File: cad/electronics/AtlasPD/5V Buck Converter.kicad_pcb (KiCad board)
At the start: 2 copper layers, 93.5 x 50.4 mm, 12 parts, among them J401 Conn_01x04, U402 AP1509-50SG-13

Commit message: KiCad 6.0 upgrade
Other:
- net class Default removed

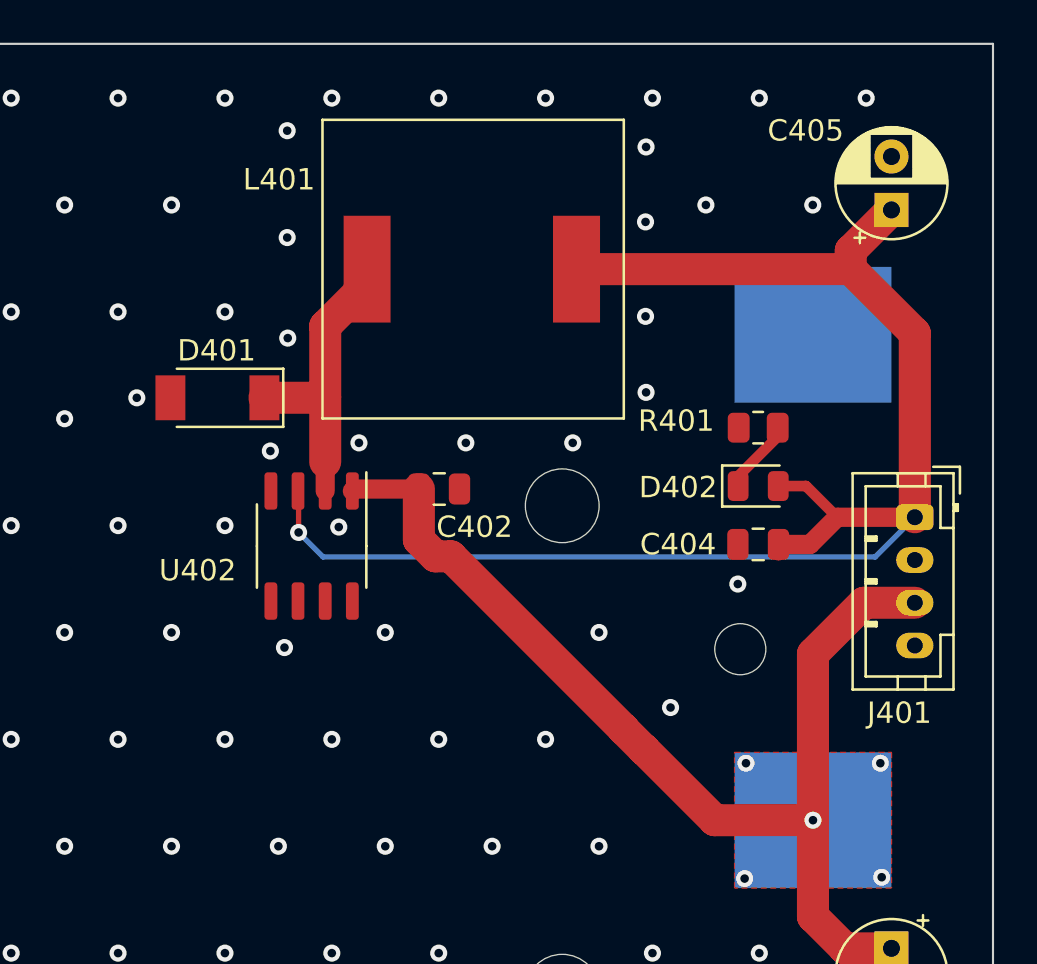
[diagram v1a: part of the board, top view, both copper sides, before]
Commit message: Started adding battery protection and fuel guage design
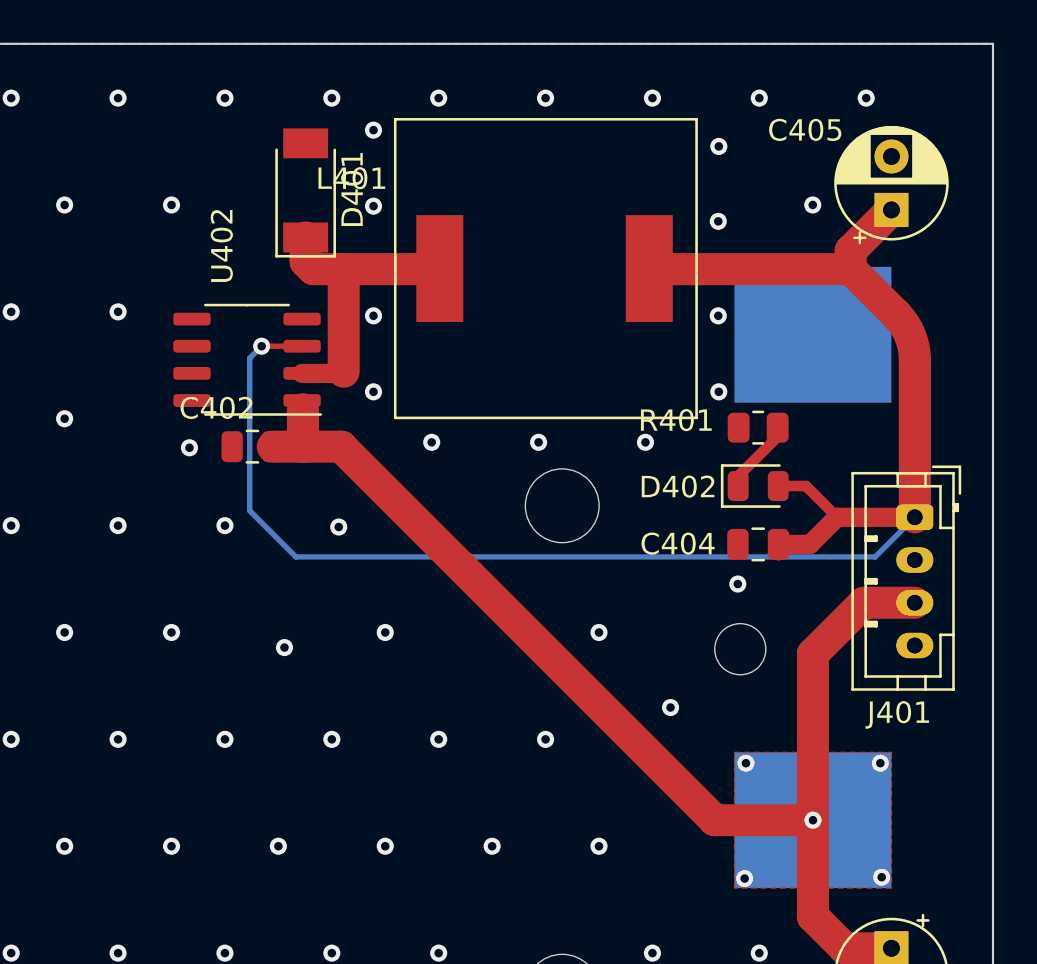
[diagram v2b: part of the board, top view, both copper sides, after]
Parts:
- moved D401 10.5 mm to (76.4, 51.3), turned to 90 degrees
- moved U402 9.22 mm to (73.7, 59.2), turned to 180 degrees
- moved C402 8.96 mm to (73.9, 63.3), turned to 180 degrees
- moved L401 3.40 mm to (87.6, 55.0)
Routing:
- net +5V: track 72.8 -> 79.1 mm
- net +BATT: track 51.7 -> 56.6 mm
- net GND: vias 144 -> 142

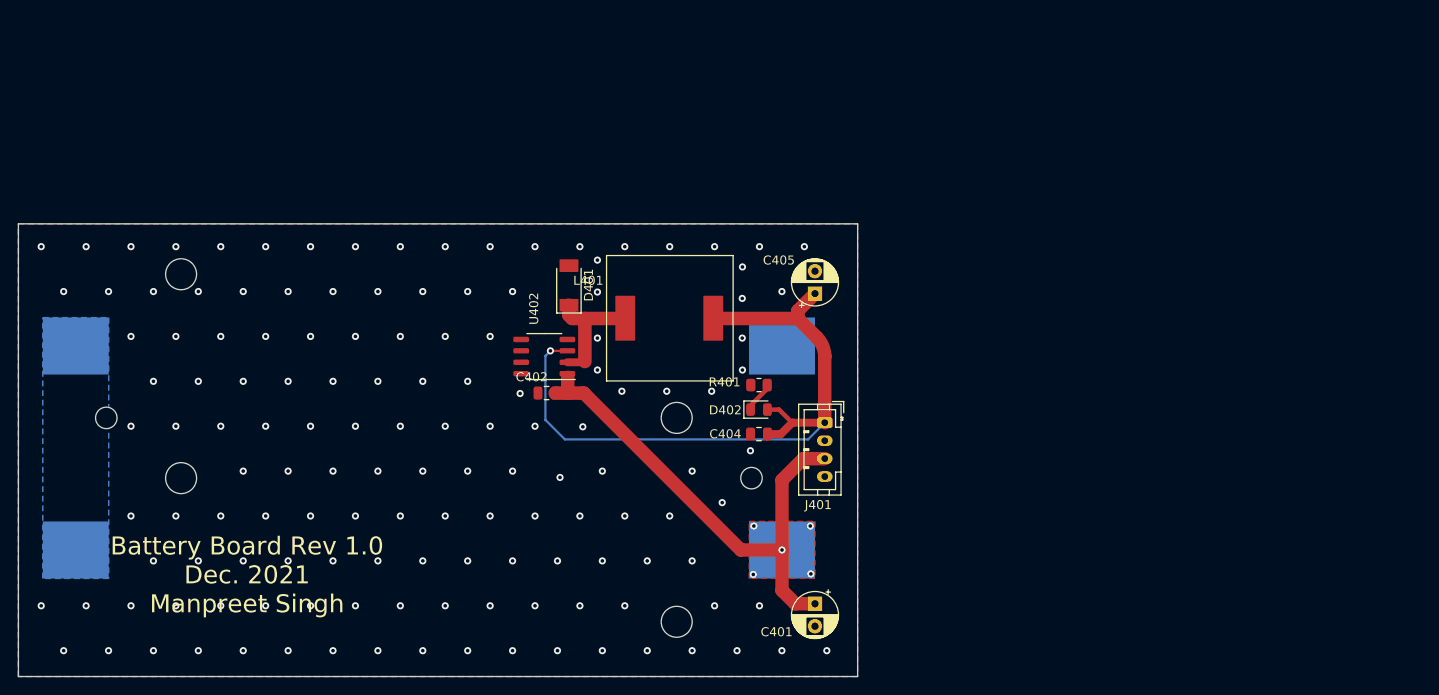
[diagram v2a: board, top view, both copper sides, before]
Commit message: Finished IC Schematic, Assigned footprints
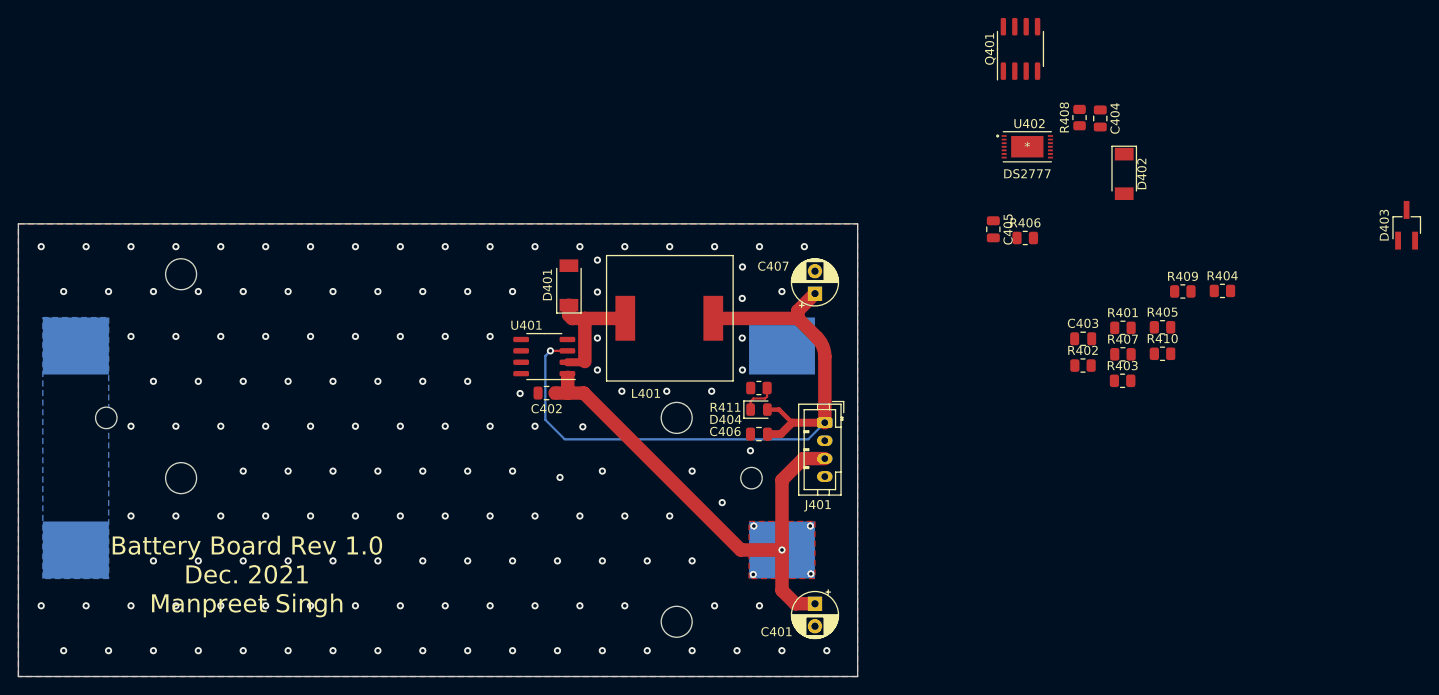
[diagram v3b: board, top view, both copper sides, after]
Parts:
- added C403: 0.1u, Capacitor_SMD:C_0805_2012Metric, F.Cu at (133.7, 57.3)
- added C404: 0.47u, Capacitor_SMD:C_0805_2012Metric, F.Cu at (135.6, 32.7)
- added C405: 0.1u, Capacitor_SMD:C_0805_2012Metric, F.Cu at (123.7, 45.1)
- added D402: D_Schottky, Diode_SMD:D_SOD-128, F.Cu at (138.3, 38.9)
- added D403: D_Zener_Dual_CommonAnode_KKA_Parallel, Package_TO_SOT_SMD:TSOT-23_HandSoldering, F.Cu at (169.7, 44.6)
- added Q401: Q_Dual_NMOS_S1G1S2G2D2D2D1D1, Package_SO:SOIC-8_3.9x4.9mm_P1.27mm, F.Cu at (126.7, 25.0)
- added R401: 1k, Resistor_SMD:R_0805_2012Metric, F.Cu at (138.1, 56.0)
- added R402: 1k, Resistor_SMD:R_0805_2012Metric, F.Cu at (133.7, 60.2)
- added R403: 150, Resistor_SMD:R_0805_2012Metric, F.Cu at (138.1, 61.9)
- added R404: 1k, Resistor_SMD:R_0805_2012Metric, F.Cu at (149.2, 51.9)
- added R405: 470, Resistor_SMD:R_0805_2012Metric, F.Cu at (142.5, 56.0)
- added R406: RSNS, Resistor_SMD:R_0805_2012Metric, F.Cu at (127.3, 46.0)
- added R407: 1k, Resistor_SMD:R_0805_2012Metric, F.Cu at (138.1, 59.0)
- added R408: 1k, Resistor_SMD:R_0805_2012Metric, F.Cu at (133.3, 32.6)
- added R409: 150, Resistor_SMD:R_0805_2012Metric, F.Cu at (144.8, 52.0)
- added R410: 150, Resistor_SMD:R_0805_2012Metric, F.Cu at (142.5, 58.9)
- added U402: DS2777, SamacSys_Parts:DS2777G+, F.Cu at (127.5, 35.9)
- moved R411 0.33 mm to (97.6, 62.7)
- renumbered C404 to C406, C405 to C407, D402 to D404, R401 to R411, U402 to U401
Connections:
- BT401 pad 1: +BATT -> Net-(BT401-Pad1)
- BT402 pad 2: GND -> GNDPWR
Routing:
- net Net-(D404-Pad1): track 3.50 -> 4.80 mm

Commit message: Forgot to save
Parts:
- moved D402 24.6 mm to (113.7, 37.8), turned to 0 degrees
- moved R407 19.4 mm to (133.7, 40.1), turned to 180 degrees
- moved D403 6.48 mm to (164.0, 41.5), turned to -90 degrees
- moved C404 5.67 mm to (133.7, 38.0), turned to 0 degrees
- moved U402 3.26 mm to (124.7, 37.5)
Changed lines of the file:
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@@
   )
   (footprint "Package_TO_SOT_SMD:TSOT-23_HandSoldering" (layer "F.Cu")
-    (at 169.7244 44.6106 90)
+    (at 164.0332 41.5036 -90)
     (descr "5-pin TSOT23 package, http://cds.linear.com/docs/en/packaging/SOT_5_05-08-1635.pdf")
     (tags "TSOT-23 Hand-soldering")
@@
     (fp_line (start -0.88 -1) (end -0.43 -1.45) (layer "F.Fab") (width 0.1))
     (fp_line (start 0.88 -1.45) (end -0.43 -1.45) (layer "F.Fab") (width 0.1))
-    (pad "1" smd rect locked (at -1.71 -0.95 90) (size 2 0.65) (layers "F.Cu" "F.Paste" "F.Mask")
+    (pad "1" smd rect locked (at -1.71 -0.95 270) (size 2 0.65) (layers "F.Cu" "F.Paste" "F.Mask")
       (net 21 "Net-(D403-Pad1)") (pinfunction "K") (pintype "passive"))
-    (pad "2" smd rect locked (at -1.71 0.95 90) (size 2 0.65) (layers "F.Cu" "F.Paste" "F.Mask")
+    (pad "2" smd rect locked (at -1.71 0.95 270) (size 2 0.65) (layers "F.Cu" "F.Paste" "F.Mask")
       (net 23 "Net-(D403-Pad2)") (pinfunction "K") (pintype "passive"))
-    (pad "3" smd rect locked (at 1.71 0 90) (size 2 0.65) (layers "F.Cu" "F.Paste" "F.Mask")
+    (pad "3" smd rect locked (at 1.71 0 270) (size 2 0.65) (layers "F.Cu" "F.Paste" "F.Mask")
       (net 1 "GND") (pinfunction "A") (pintype "passive"))
     (model "${KICAD6_3DMODEL_DIR}/Package_TO_SOT_SMD.3dshapes/TSOT-23.wrl"
@@
   )
   (footprint "Diode_SMD:D_SOD-128" (layer "F.Cu")
-    (at 138.2776 38.8874 -90)
+    (at 113.665 37.7698)
     (descr "D_SOD-128 (CFP5 SlimSMAW), https://assets.nexperia.com/documents/outline-drawing/SOD128.pdf")
     (tags "D_SOD-128")
@@
     (property "Sheetname" "")
     (attr smd)
-    (fp_text reference "D402" (at 0 -2 90) (layer "F.SilkS")
-      (effects (font (size 1 1) (thickness 0.15)))
-    )
-    (fp_text value "D_Schottky" (at 0 2 90) (layer "F.Fab")
-      (effects (font (size 1 1) (thickness 0.15)))
-    )
-    (fp_text user "${REFERENCE}" (at 0 -2 90) (layer "F.Fab")
+    (fp_text reference "D402" (at 0 -2) (layer "F.SilkS")
+      (effects (font (size 1 1) (thickness 0.15)))
+    )
+    (fp_text value "D_Schottky" (at 0 2) (layer "F.Fab")
+      (effects (font (size 1 1) (thickness 0.15)))
+    )
+    (fp_text user "${REFERENCE}" (at 0 -2) (layer "F.Fab")
       (effects (font (size 1 1) (thickness 0.15)))
     )
@@
     (fp_line (start 1.9 1.25) (end -1.9 1.25) (layer "F.Fab") (width 0.1))
     (fp_line (start -0.35 0) (end -0.35 0.55) (layer "F.Fab") (width 0.1))
-    (pad "1" smd rect locked (at -2.2 0 270) (size 1.4 2.1) (layers "F.Cu" "F.Paste" "F.Mask")
+    (pad "1" smd rect locked (at -2.2 0) (size 1.4 2.1) (layers "F.Cu" "F.Paste" "F.Mask")
       (net 5 "Net-(D402-Pad1)") (pinfunction "K") (pintype "passive"))
-    (pad "2" smd rect locked (at 2.2 0 270) (size 1.4 2.1) (layers "F.Cu" "F.Paste" "F.Mask")
+    (pad "2" smd rect locked (at 2.2 0) (size 1.4 2.1) (layers "F.Cu" "F.Paste" "F.Mask")
       (net 1 "GND") (pinfunction "A") (pintype "passive"))
     (model "${KICAD6_3DMODEL_DIR}/Diode_SMD.3dshapes/D_SOD-128.wrl"
@@
   )
   (footprint "Resistor_SMD:R_0805_2012Metric" (layer "F.Cu")
-    (at 138.1356 58.9816)
+    (at 133.6802 40.0558 180)
     (descr "Resistor SMD 0805 (2012 Metric), square (rectangular) end terminal, IPC_7351 nominal, (Body size source: IPC-SM-782 page 72, https://www.pcb-3d.com/wordpress/wp-content/uploads/ipc-sm-782a_amendment_1_and_2.pdf), generated with kicad-footprint-generator")
     (tags "resistor")
@@
     (fp_line (start 1 0.625) (end -1 0.625) (layer "F.Fab") (width 0.1))
     (fp_line (start 1 -0.625) (end 1 0.625) (layer "F.Fab") (width 0.1))
-    (pad "1" smd roundrect locked (at -0.9125 0) (size 1.025 1.4) (layers "F.Cu" "F.Paste" "F.Mask") (roundrect_rratio 0.243902)
+    (pad "1" smd roundrect locked (at -0.9125 0 180) (size 1.025 1.4) (layers "F.Cu" "F.Paste" "F.Mask") (roundrect_rratio 0.243902)
       (net 19 "Net-(Q401-Pad2)") (pintype "passive"))
-    (pad "2" smd roundrect locked (at 0.9125 0) (size 1.025 1.4) (layers "F.Cu" "F.Paste" "F.Mask") (roundrect_rratio 0.243902)
+    (pad "2" smd roundrect locked (at 0.9125 0 180) (size 1.025 1.4) (layers "F.Cu" "F.Paste" "F.Mask") (roundrect_rratio 0.243902)
       (net 20 "Net-(R407-Pad2)") (pintype "passive"))
     (model "${KICAD6_3DMODEL_DIR}/Resistor_SMD.3dshapes/R_0805_2012Metric.wrl"
@@
   )
   (footprint "Capacitor_SMD:C_0805_2012Metric" (layer "F.Cu")
-    (at 135.6106 32.7152 -90)
+    (at 133.6802 38.0492)
     (descr "Capacitor SMD 0805 (2012 Metric), square (rectangular) end terminal, IPC_7351 nominal, (Body size source: IPC-SM-782 page 76, https://www.pcb-3d.com/wordpress/wp-content/uploads/ipc-sm-782a_amendment_1_and_2.pdf, https://docs.google.com/spreadsheets/d/1BsfQQcO9C6DZCsRaXUlFlo91Tg2WpOkGARC1WS5S8t0/edit?usp=sharing), generated with kicad-footprint-generator")
     (tags "capacitor")
@@
     (property "Sheetname" "")
     (attr smd)
-    (fp_text reference "C404" (at 0 -1.68 90) (layer "F.SilkS")
-      (effects (font (size 1 1) (thickness 0.15)))
-    )
-    (fp_text value "0.47u" (at 0 1.68 90) (layer "F.Fab")
-      (effects (font (size 1 1) (thickness 0.15)))
-    )
-    (fp_text user "${REFERENCE}" (at 0 0 90) (layer "F.Fab")
+    (fp_text reference "C404" (at 0 -1.68) (layer "F.SilkS")
+      (effects (font (size 1 1) (thickness 0.15)))
+    )
+    (fp_text value "0.47u" (at 0 1.68) (layer "F.Fab")
+      (effects (font (size 1 1) (thickness 0.15)))
+    )
+    (fp_text user "${REFERENCE}" (at 0 0) (layer "F.Fab")
       (effects (font (size 0.5 0.5) (thickness 0.08)))
     )
@@
     (fp_line (start -1 0.625) (end -1 -0.625) (layer "F.Fab") (width 0.1))
     (fp_line (start 1 0.625) (end -1 0.625) (layer "F.Fab") (width 0.1))
-    (pad "1" smd roundrect locked (at -0.95 0 270) (size 1 1.45) (layers "F.Cu" "F.Paste" "F.Mask") (roundrect_rratio 0.25)
+    (pad "1" smd roundrect locked (at -0.95 0) (size 1 1.45) (layers "F.Cu" "F.Paste" "F.Mask") (roundrect_rratio 0.25)
       (net 10 "Net-(C404-Pad1)") (pintype "passive"))
-    (pad "2" smd roundrect locked (at 0.95 0 270) (size 1 1.45) (layers "F.Cu" "F.Paste" "F.Mask") (roundrect_rratio 0.25)
+    (pad "2" smd roundrect locked (at 0.95 0) (size 1 1.45) (layers "F.Cu" "F.Paste" "F.Mask") (roundrect_rratio 0.25)
       (net 11 "/SRC") (pintype "passive"))
     (model "${KICAD6_3DMODEL_DIR}/Capacitor_SMD.3dshapes/C_0805_2012Metric.wrl"
@@
   )
   (footprint "SamacSys_Parts:DS2777G+" (layer "F.Cu")
-    (at 127.4826 35.8648)
-    (property "Sheetfile" "5V Buck Converter.kicad_sch")
-    (property "Sheetname" "")
+    (at 124.677501 37.521323)
+    (property "Sheetfile" "5V Buck Converter.kicad_sch")
+    (property "Sheetname" "")

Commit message: Fixed schematic issues from KiCAD upgrade, Moved 3.3V LDO to MCU Sheet
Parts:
- added TP401: SDA, TestPoint:TestPoint_Pad_1.5x1.5mm, F.Cu at (68.3, 85.2)
- added TP402: SCL, TestPoint:TestPoint_Pad_D1.5mm, F.Cu at (68.2, 82.4)
- moved D403 97.2 mm to (76.7, 84.2), turned to 0 degrees
- moved R409 79.1 mm to (72.0, 82.9), turned to 180 degrees
- moved R410 75.4 mm to (71.9, 85.3), turned to 180 degrees
- moved R404 69.7 mm to (84.3, 77.2), turned to 180 degrees
- moved R401 68.8 mm to (70.7, 69.6)
- moved R406 66.1 mm to (67.5, 74.3), turned to 180 degrees
- moved R405 65.8 mm to (79.6, 75.1)
- moved U402 64.8 mm to (74.2, 78.2), turned to 180 degrees
- moved C404 63.5 mm to (80.3, 72.5)
- moved Q401 63.3 mm to (90.7, 77.1), turned to 0 degrees
- moved R407 63.0 mm to (84.3, 79.2)
- moved R408 60.0 mm to (87.6, 71.5), turned to 180 degrees
- moved R403 58.1 mm to (84.7, 84.8)
- moved C405 55.2 mm to (75.9, 72.6), turned to 0 degrees
- moved C403 52.7 mm to (88.8, 84.8)
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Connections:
- net Net-(BT401-Pad1) renamed /BT_VDD
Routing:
- net +BATT: track 56.6 -> 10.7 mm, vias 5 -> 0
- net Net-(D403-Pad2): vias 0 -> 1
- net GND: vias 142 -> 129
- net /BT_VDD: vias 0 -> 5

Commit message: Small changes, saving what I have
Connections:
- Q401 pad 1: Net-(Q401-Pad1) -> /SRC
- Q401 pad 3: Net-(Q401-Pad1) -> /SRC
- R405 pad 1: Net-(Q401-Pad1) -> /SRC
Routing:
- net +BATT: track 10.7 -> 19.1 mm
- net /BT_VDD: track 0.00 -> 7.71 mm
- net Net-(D403-Pad2): vias 1 -> 0
- net GND: vias 129 -> 130
- added copper zone on F.Cu, net /BT_VDD
- added copper zone on F.Cu, net /SRC

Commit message: Finished Battery Board V2 PCB Layout
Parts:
- added REF**: OSHW-Symbol_6.7x6mm_SilkScreen, Symbol:OSHW-Symbol_6.7x6mm_SilkScreen, F.Cu at (21.6, 73.8)
- added REF**: Symbol_GNU-Logo_SilkscreenTop, Symbol:Symbol_GNU-Logo_SilkscreenTop, F.Cu at (22.7, 56.9)
- moved D402 17.9 mm to (67.6, 74.8), turned to 90 degrees
- moved D403 16.7 mm to (62.7, 75.2), turned to 90 degrees
- moved R409 11.0 mm to (61.4, 80.0), turned to -90 degrees
- moved R410 9.71 mm to (63.8, 80.0), turned to -90 degrees
- moved C403 8.89 mm to (80.0, 83.7), turned to 180 degrees
- moved TP402 7.25 mm to (61.1, 83.7), turned to 90 degrees
- moved R401 6.90 mm to (77.5, 71.0), turned to -90 degrees
- moved R406 6.74 mm to (74.2, 75.3)
- moved R402 6.63 mm to (84.1, 81.6)
- moved R408 5.46 mm to (82.2, 71.0), turned to 90 degrees
- moved R405 5.13 mm to (84.1, 77.6), turned to 180 degrees
- moved TP401 4.60 mm to (64.0, 83.6), turned to 90 degrees
- moved R407 3.69 mm to (84.1, 75.5)
- moved R404 2.42 mm to (84.1, 79.6)
- moved C405 1.66 mm to (75.3, 71.0), turned to 90 degrees
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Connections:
- Q401 pad 1: /SRC -> /Q_SRC
- Q401 pad 3: /SRC -> /Q_SRC
- R405 pad 1: /SRC -> /Q_SRC
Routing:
- net Net-(BT401-Pad2): track 0.00 -> 54.9 mm, vias 0 -> 1
- net +BATT: track 19.1 -> 68.2 mm
- net /SRC: track 0.00 -> 32.0 mm, vias 0 -> 2
- net Net-(D402-Pad1): track 0.00 -> 24.8 mm, vias 0 -> 2
- net Net-(C404-Pad1): track 0.00 -> 17.1 mm, vias 0 -> 2
- net Net-(D403-Pad1): track 0.00 -> 13.5 mm
- net Net-(R407-Pad2): track 0.00 -> 12.2 mm, vias 0 -> 2
- net /BT_VDD: track 7.71 -> 19.5 mm
- net +5V: track 79.1 -> 67.4 mm, vias 1 -> 2
- net Net-(D403-Pad2): track 0.00 -> 10.8 mm
- net Net-(R402-Pad2): track 0.00 -> 10.7 mm
- net GNDPWR: track 0.00 -> 10.1 mm, vias 0 -> 11
- net Net-(C403-Pad1): track 0.00 -> 10.0 mm
- net Net-(C405-Pad1): track 0.00 -> 9.45 mm
- net Net-(R401-Pad2): track 0.00 -> 8.40 mm
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- added copper zone on F.Cu, net /Q_SRC
- added copper zone on B.Cu, net GNDPWR
- added copper zone on F.Cu, net GNDPWR
- removed copper zone on F.Cu, net /SRC
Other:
- board text added: "Battery Board Rev 2.0"
- board text added: "Jan. 2022"
- board text added: "Manpreet Singh"
- board text removed: "Battery Board Rev 1.0 Dec. 2021 Manpreet Singh"

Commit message: Small Tweaks
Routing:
- net +5V: track 67.4 -> 68.4 mm
- net GNDPWR: vias 11 -> 14
- net GND: vias 125 -> 123
